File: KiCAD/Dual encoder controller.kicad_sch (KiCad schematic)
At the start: 8 parts, among them J1 8P8C_Shielded, J2 8P8C_Shielded, J4 2.5x5.5 Barrel Jack, SW1 B3J-3300, U8 Itsy_Bitsy_32u4

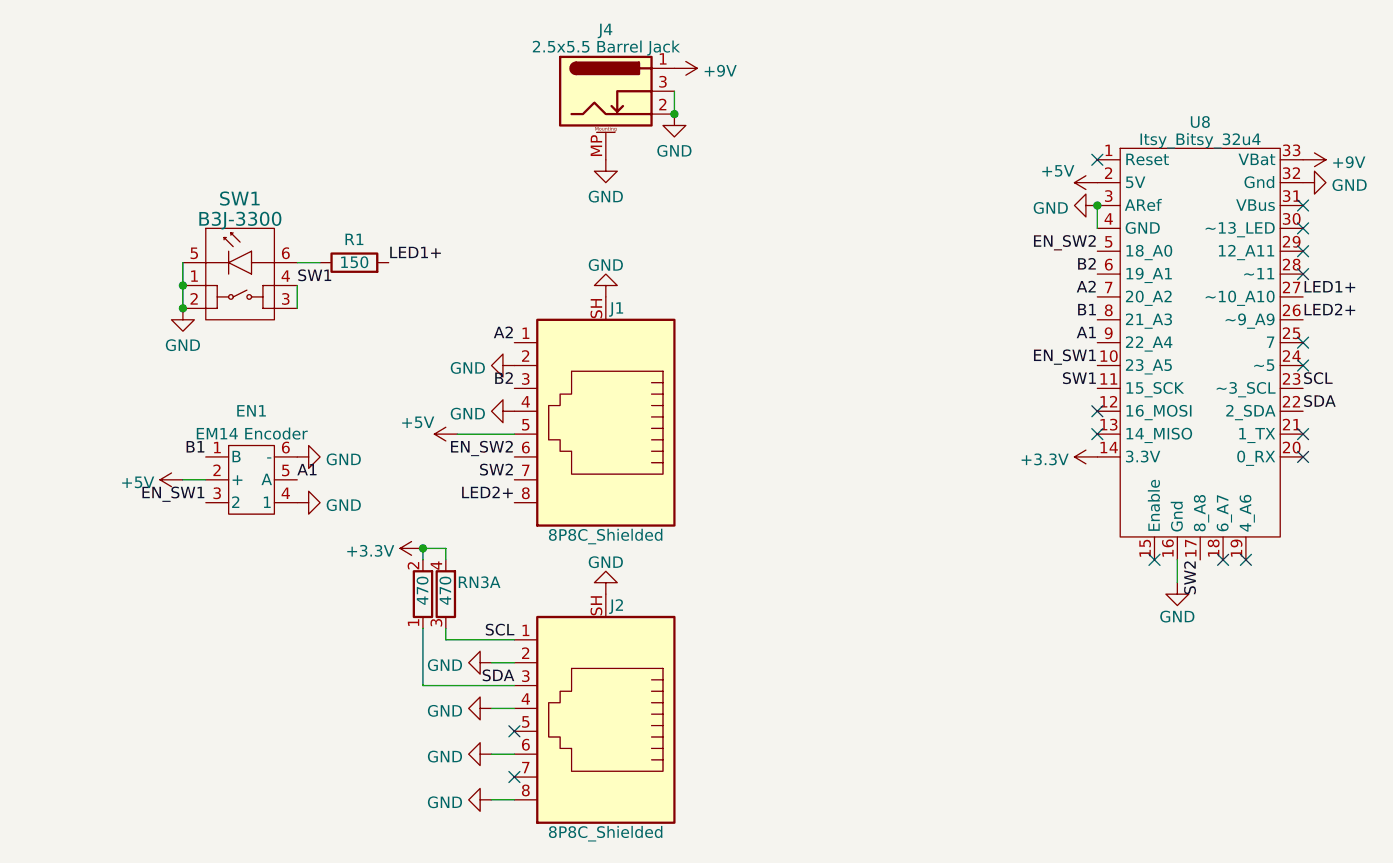
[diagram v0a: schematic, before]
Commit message: Add encoder bypass and guard vias
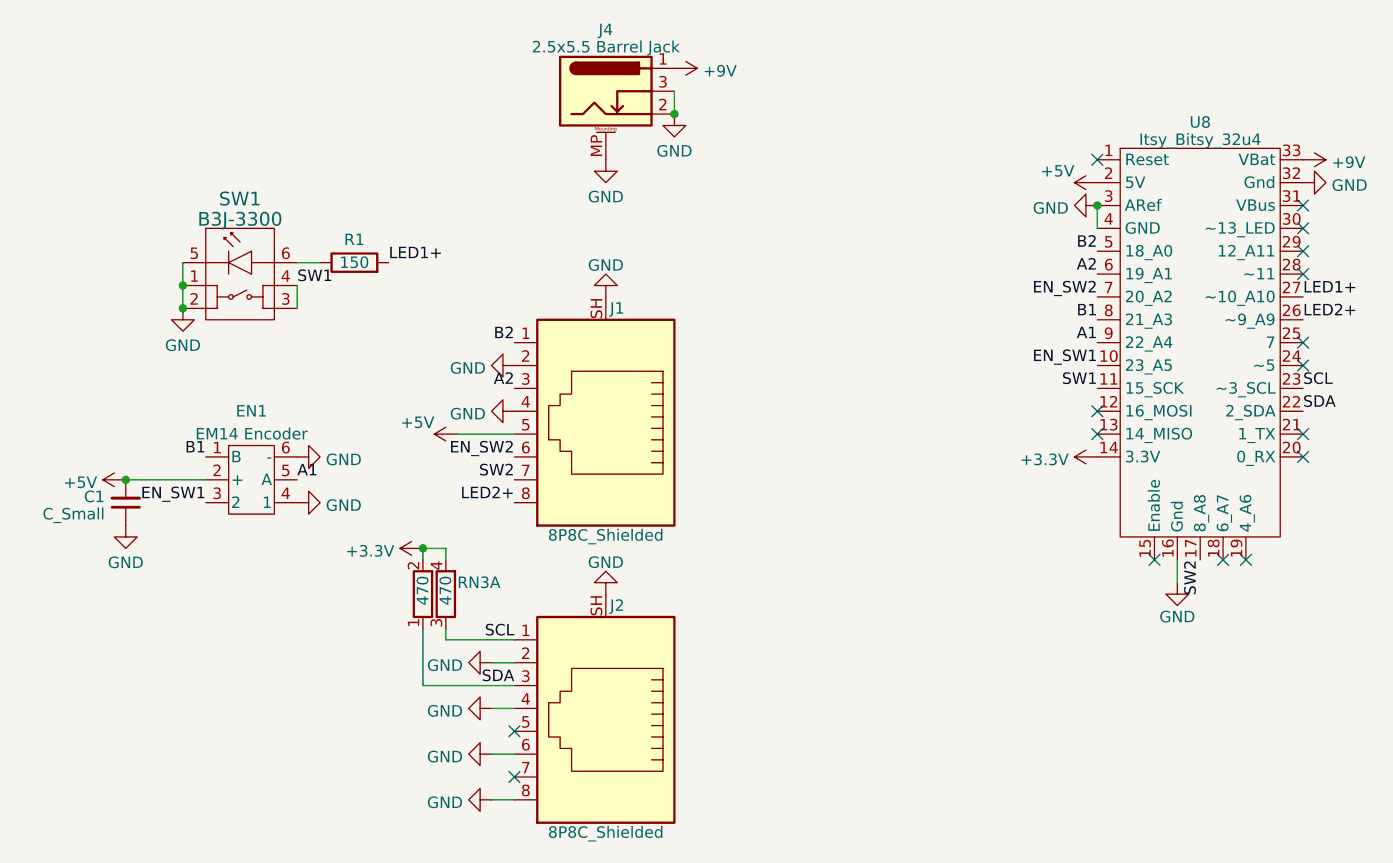
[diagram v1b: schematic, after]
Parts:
- added C1: C_Small, Capacitor_THT:C_Rect_L4.0mm_W2.5mm_P2.50mm, symbol Device:C_Small
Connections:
- net +5V: now also C1.2
- net A2: now also J1.3, U8.6 (19_A1); no longer J1.1, U8.7 (20_A2)
- net B2: now also J1.1, U8.5 (18_A0); no longer J1.3, U8.6 (19_A1)
- net EN_SW2: now also U8.7 (20_A2); no longer U8.5 (18_A0)
- net GND: now also C1.1
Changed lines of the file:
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@@
   (junction (at 165.1 48.26) (diameter 0) (color 0 0 0 0)
+  )
+  (junction (at 104.14 88.9) (diameter 0) (color 0 0 0 0)
   )
   (junction (at 110.49 69.85) (diameter 0) (color 0 0 0 0)
@@
     (stroke (width 0) (type default))
   )
-  (wire (pts (xy 110.49 88.9) (xy 113.03 88.9))
+  (wire (pts (xy 104.14 88.9) (xy 113.03 88.9))
     (stroke (width 0) (type default))
   )
@@
     (effects (font (size 1.27 1.27)) (justify left bottom))
   )
-  (label "A2" (at 212.09 68.58 180) (fields_autoplaced)
+  (label "A2" (at 212.09 66.04 180) (fields_autoplaced)
     (effects (font (size 1.27 1.27)) (justify right bottom))
   )
@@
     (effects (font (size 1.27 1.27)) (justify left bottom))
   )
-  (label "A2" (at 147.32 73.66 180) (fields_autoplaced)
-    (effects (font (size 1.27 1.27)) (justify right bottom))
-  )
-  (label "B2" (at 147.32 78.74 180) (fields_autoplaced)
+  (label "A2" (at 147.32 78.74 180) (fields_autoplaced)
+    (effects (font (size 1.27 1.27)) (justify right bottom))
+  )
+  (label "B2" (at 147.32 73.66 180) (fields_autoplaced)
     (effects (font (size 1.27 1.27)) (justify right bottom))
   )
@@
     (effects (font (size 1.27 1.27)) (justify right bottom))
   )
-  (label "B2" (at 212.09 66.04 180) (fields_autoplaced)
+  (label "B2" (at 212.09 63.5 180) (fields_autoplaced)
     (effects (font (size 1.27 1.27)) (justify right bottom))
   )
@@
     (effects (font (size 1.27 1.27)) (justify right bottom))
   )
-  (label "EN_SW2" (at 212.09 63.5 180) (fields_autoplaced)
+  (label "EN_SW2" (at 212.09 68.58 180) (fields_autoplaced)
     (effects (font (size 1.27 1.27)) (justify right bottom))
   )
@@
     )
   )
+  (symbol (lib_id "power:GND") (at 104.14 93.98 0) (unit 1)
+    (in_bom yes) (on_board yes) (dnp no) (fields_autoplaced)
+    (property "Reference" "#PWR024" (at 104.14 100.33 0)
+      (effects (font (size 1.27 1.27)) hide)
+    )
+    (property "Value" "GND" (at 104.14 98.1155 0)
+      (effects (font (size 1.27 1.27)))
+    )
+    (property "Footprint" "" (at 104.14 93.98 0)
+      (effects (font (size 1.27 1.27)) hide)
+    )
+    (property "Datasheet" "" (at 104.14 93.98 0)
+      (effects (font (size 1.27 1.27)) hide)
+    )
+    (pin "1")
+    (instances
+      (project "Dual encoder controller"
+        (path "/f63253f1-d78d-4fac-a266-90df8fae5286"
+          (reference "#PWR024") (unit 1)
+        )
+      )
+    )
+  )
   (symbol (lib_id "Connector:Barrel_Jack_Switch_MountingPin") (at 157.48 45.72 0) (unit 1)
     (in_bom yes) (on_board yes) (dnp no) (fields_autoplaced)
@@
     )
   )
-  (symbol (lib_id "power:+5V") (at 110.49 88.9 90) (unit 1)
-    (in_bom yes) (on_board yes) (dnp no) (fields_autoplaced)
-    (property "Reference" "#PWR01" (at 114.3 88.9 0)
-      (effects (font (size 1.27 1.27)) hide)
-    )
-    (property "Value" "+5V" (at 107.3151 89.2168 90)
+  (symbol (lib_id "power:+5V") (at 104.14 88.9 90) (unit 1)
+    (in_bom yes) (on_board yes) (dnp no) (fields_autoplaced)
+    (property "Reference" "#PWR01" (at 107.95 88.9 0)
+      (effects (font (size 1.27 1.27)) hide)
+    )
+    (property "Value" "+5V" (at 100.9651 89.2168 90)
       (effects (font (size 1.27 1.27)) (justify left))
     )
-    (property "Footprint" "" (at 110.49 88.9 0)
-      (effects (font (size 1.27 1.27)) hide)
-    )
-    (property "Datasheet" "" (at 110.49 88.9 0)
+    (property "Footprint" "" (at 104.14 88.9 0)
+      (effects (font (size 1.27 1.27)) hide)
+    )
+    (property "Datasheet" "" (at 104.14 88.9 0)
       (effects (font (size 1.27 1.27)) hide)
     )
@@
         )
       )
+    )
+  )
+  (symbol (lib_id "Device:C_Small") (at 104.14 91.44 0) (mirror x) (unit 1)
+    (in_bom yes) (on_board yes) (dnp no) (fields_autoplaced)
+    (property "Reference" "C1" (at 101.8159 90.7899 0)
+      (effects (font (size 1.27 1.27)) (justify right))
+    )
+    (property "Value" "C_Small" (at 101.8159 92.7109 0)
+      (effects (font (size 1.27 1.27)) (justify right))
+    )
+    (property "Footprint" "Capacitor_THT:C_Rect_L4.0mm_W2.5mm_P2.50mm" (at 104.14 91.44 0)
+      (effects (font (size 1.27 1.27)) hide)
+    )
+    (property "Datasheet" "https://search.murata.co.jp/Ceramy/image/img/A01X/G101/ENG/RCE_X7R_X7S_25V-100V_E.pdf" (at 104.14 91.44 0)
+      (effects (font (size 1.27 1.27)) hide)
+    )
+    (property "Manufacturer" "Murata Electronics" (at 104.14 91.44 0)
+      (effects (font (size 1.27 1.27)) hide)
+    )
+    (property "Part" "RCER71H105K2DBH03A" (at 104.14 91.44 0)
+      (effects (font (size 1.27 1.27)) hide)
+    )
+    (pin "1")
+    (pin "2")
+    (instances
+      (project "Dual encoder controller"
+        (path "/f63253f1-d78d-4fac-a266-90df8fae5286"
+          (reference "C1") (unit 1)
+        )
+      )
